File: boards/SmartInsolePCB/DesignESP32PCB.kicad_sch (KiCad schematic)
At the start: 59 parts, among them J1 PJS008U-3000-0, J10 Conn_01x02_Pin, J11 Conn_01x02_Pin, J12 Conn_01x02_Pin, J13 Conn_01x05_Socket, J2 Conn_01x02_Pin, J3 Conn_01x02_Pin, J4 Conn_01x02_Pin, J5 Conn_01x02_Pin, J6 Conn_01x02_Pin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

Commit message: added footprint
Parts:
- added U2: ESP32-S3-WROOM-1, RF_Module:ESP32-S3-WROOM-1, symbol RF_Module:ESP32-S3-WROOM-1
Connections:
- net 3V3: now also U2.2 (3V3)
- net CS: now also U2.21 (IO13)
- net ESP32_EN: now also U2.3 (EN)
- net End Hike: now also U2.35 (IO42)
- net GND: now also U2.1 (GND), U2.40 (GND), U2.41 (GND)
- net GPIO0_STRAPPING: now also U2.27 (IO0)
- net GPIO1: now also U2.10 (IO17)
- net GPIO10: now also U2.23 (IO21)
- net GPIO11: now also U2.20 (IO12)
- net GPIO12: now also U2.7 (IO7)
- net GPIO2: now also U2.11 (IO18)
- net GPIO21: now also U2.12 (IO8)
- net GPIO3: now also U2.19 (IO11)
- net GPIO3_STRAPPING: now also U2.15 (IO3)
- net GPIO46_STRAPPING: now also U2.16 (IO46)
- net GPIO47: now also U2.24 (IO47)
- net GPIO6: now also U2.18 (IO10)
- net GPIO7: now also U2.17 (IO9)
- net GPIO8: now also U2.6 (IO6)
- net MISO: now also U2.9 (IO16)
- net MOSI: now also U2.22 (IO14)
- net RX: now also U2.36 (RXD0)
- net SCLK: now also U2.8 (IO15)
- net SCL_6050: now also U2.13 (IO19), U2.14 (IO20)
- net Start Hike: now also U2.34 (IO41)
- net TX: now also U2.37 (TXD0)
- net USB_N: now also U2.26 (IO45)
- net USB_P: now also U2.25 (IO48)
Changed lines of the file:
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@@
+	)
+	(symbol
+		(lib_id "RF_Module:ESP32-S3-WROOM-1")
+		(at 153.67 60.96 0)
+		(unit 1)
+		(exclude_from_sim no)
+		(in_bom yes)
+		(on_board yes)
+		(dnp no)
+		(fields_autoplaced yes)
+		(property "Reference" "U2"
+			(at 155.8641 30.48 0)
+			(effects
+				(font
+					(size 1.27 1.27)
+				)
+				(justify left)
+			)
+		)
+		(property "Value" "ESP32-S3-WROOM-1"
+			(at 155.8641 33.02 0)
+			(effects
+				(font
+					(size 1.27 1.27)
+				)
+				(justify left)
+			)
+		)
+		(property "Footprint" "RF_Module:ESP32-S3-WROOM-1"
+			(at 153.67 58.42 0)
+			(effects
+				(font
+					(size 1.27 1.27)
+				)
+				(hide yes)
+			)
+		)
+		(property "Datasheet" "https://www.espressif.com/sites/default/files/documentation/esp32-s3-wroom-1_wroom-1u_datasheet_en.pdf"
+			(at 153.67 60.96 0)
+			(effects
+				(font
+					(size 1.27 1.27)
+				)
+				(hide yes)
+			)
+		)
+		(property "Description" "RF Module, ESP32-S3 SoC, Wi-Fi 802.11b/g/n, Bluetooth, BLE, 32-bit, 3.3V, onboard antenna, SMD"
+			(at 153.67 60.96 0)
+			(effects
+				(font
+					(size 1.27 1.27)
+				)
+				(hide yes)
+			)
+		)
+		(pin "26"
+		)
+		(pin "1"
+		)
+		(pin "17"
+		)
+		(pin "18"
+		)
+		(pin "29"
+		)
+		(pin "5"
+		)
+		(pin "37"
+		)
+		(pin "9"
+		)
+		(pin "22"
+		)
+		(pin "36"
+		)
+		(pin "24"
+		)
+		(pin "16"
+		)
+		(pin "12"
+		)
+		(pin "21"
+		)
+		(pin "11"
+		)
+		(pin "39"
+		)
+		(pin "32"
+		)
+		(pin "31"
+		)
+		(pin "41"
+		)
+		(pin "13"
+		)
+		(pin "15"
+		)
+		(pin "28"
+		)
+		(pin "20"
+		)
+		(pin "6"
+		)
+		(pin "2"
+		)
+		(pin "14"
+		)
+		(pin "30"
+		)
+		(pin "40"
+		)
+		(pin "3"
+		)
+		(pin "38"
+		)
+		(pin "7"
+		)
+		(pin "8"
+		)
+		(pin "10"
+		)
+		(pin "34"
+		)
+		(pin "23"
+		)
+		(pin "25"
+		)
+		(pin "33"
+		)
+		(pin "27"
+		)
+		(pin "19"
+		)
+		(pin "4"
+		)
+		(pin "35"
+		)
+		(instances
+			(project "DesignESP32PCB"
+				(path "/6ab99d2f-b2da-4c6e-b437-3c51d85d9865"
+					(reference "U2")
+					(unit 1)
+				)
+			)
+		)
 	)
 	(symbol

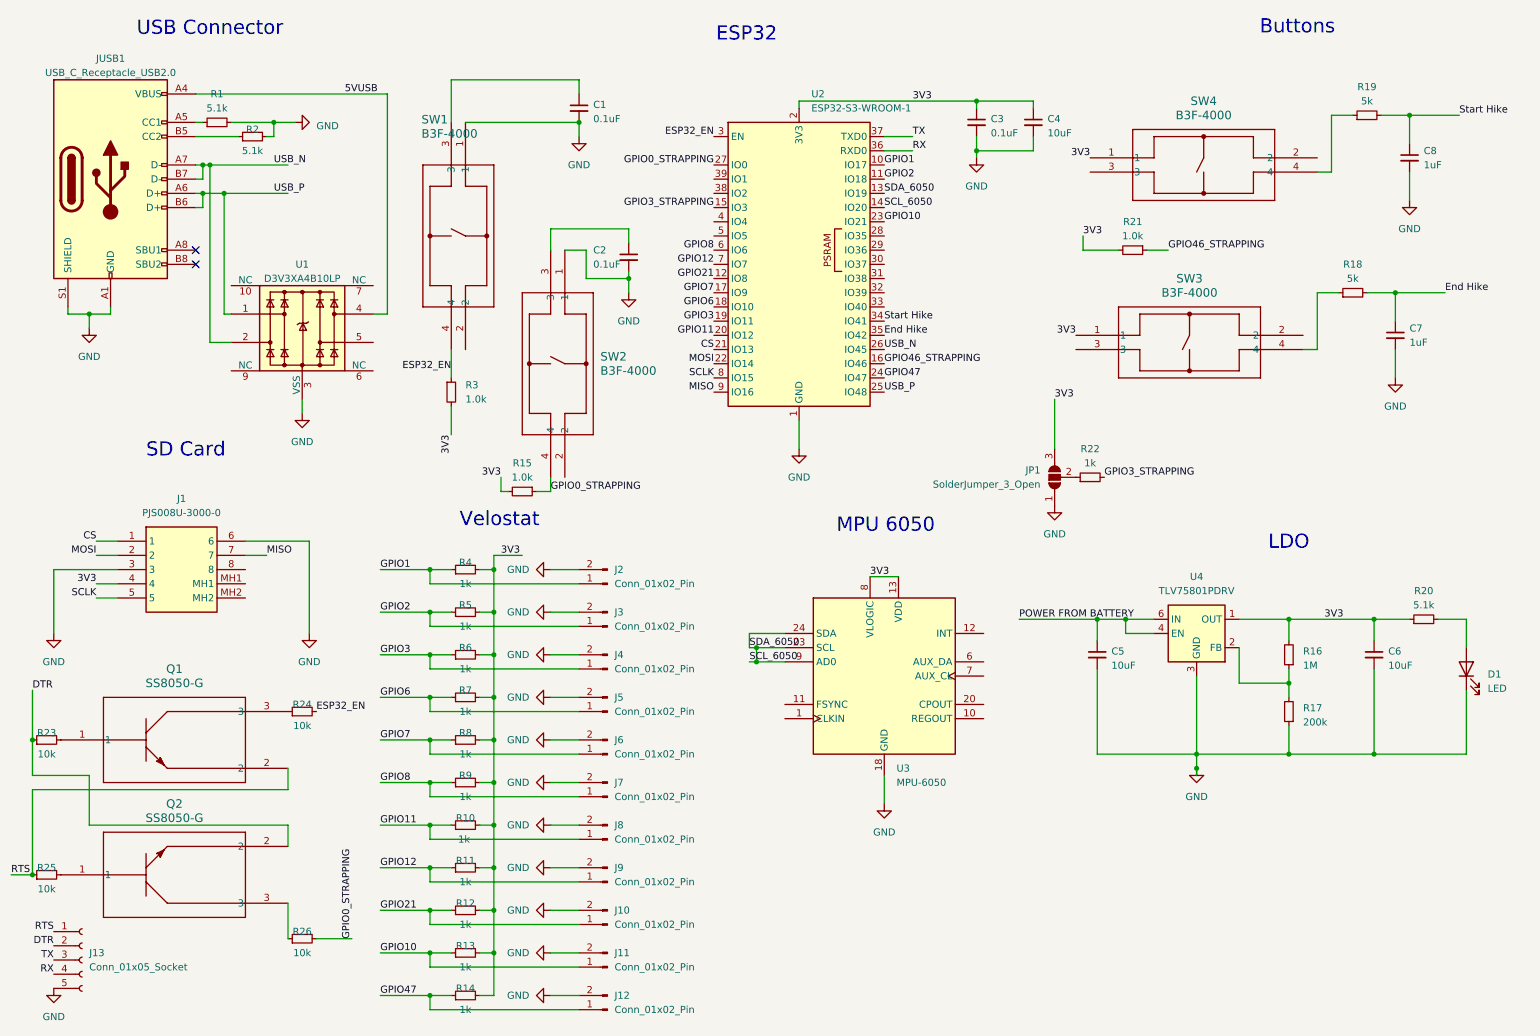
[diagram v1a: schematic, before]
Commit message: routed all connections
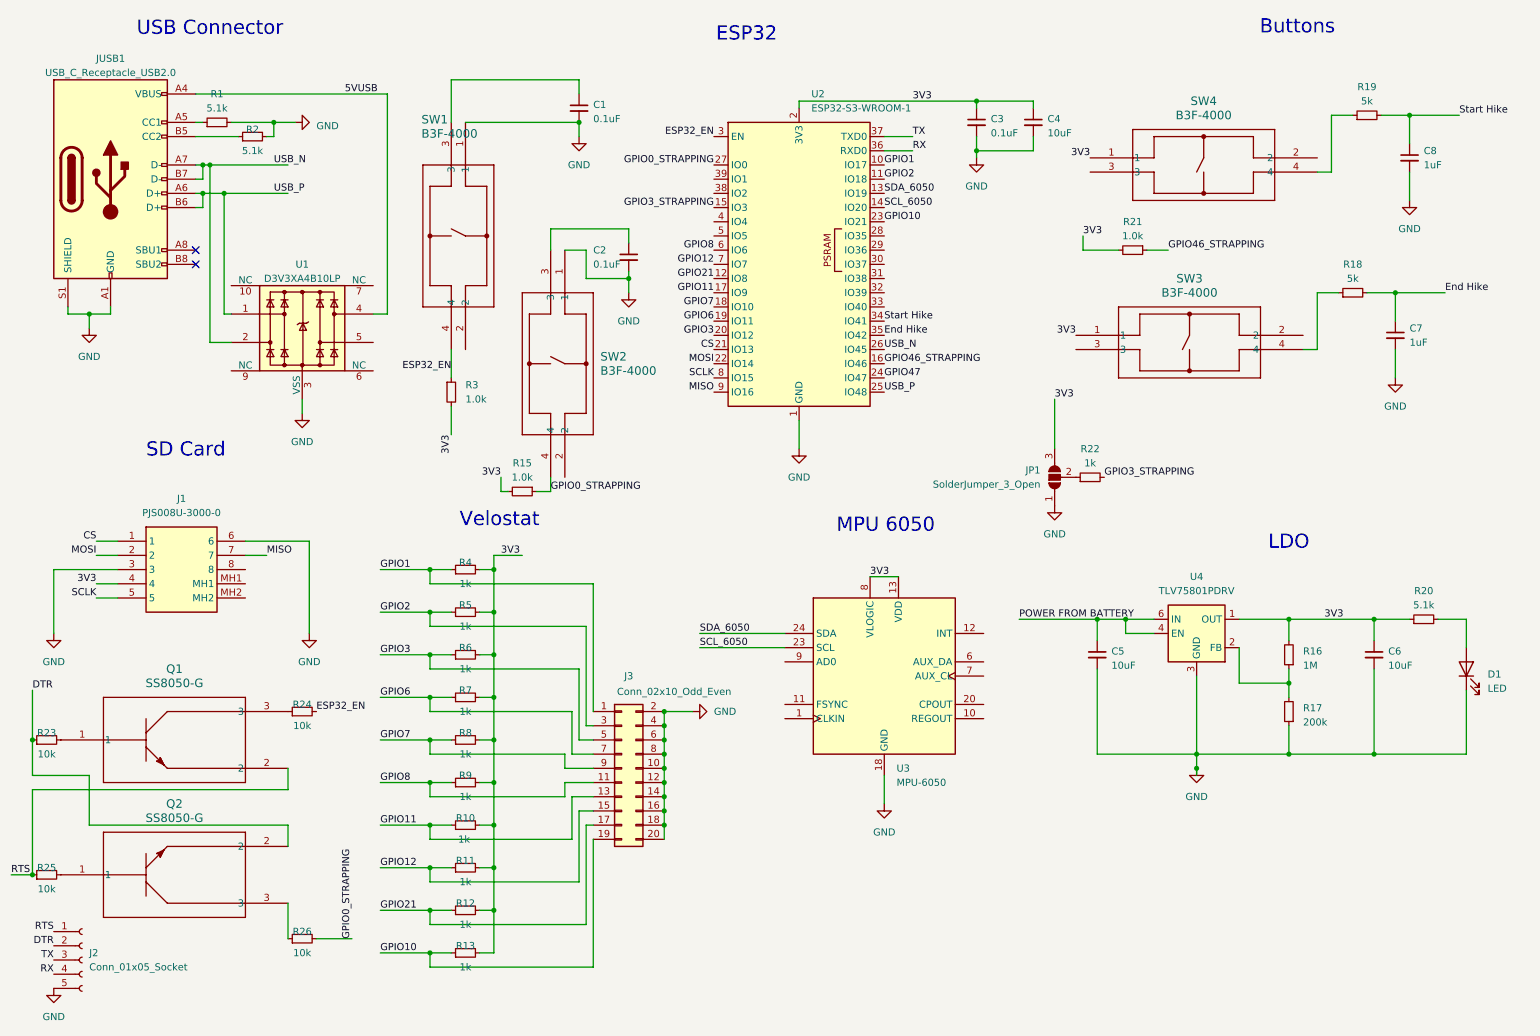
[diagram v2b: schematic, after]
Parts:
- removed J10, J11, J12, J2, J3, J4, J5, J6, J7, J8, J9: Conn_01x02_Pin, Connector_PinHeader_1.00mm:PinHeader_1x02_P1.00mm_Vertical, symbol Connector:Conn_01x02_Pin
- removed R14: 1k, Resistor_SMD:R_0603_1608Metric, symbol Device:R_Small
- added J3: Conn_02x10_Odd_Even, Connector_PinHeader_2.54mm:PinHeader_2x10_P2.54mm_Vertical, symbol Connector_Generic:Conn_02x10_Odd_Even
- J2: renamed from J13; footprint Connector_PinHeader_1.00mm:PinHeader_1x05_P1.00mm_Vertical_SMD_Pin1Left -> Connector_PinHeader_2.54mm:PinHeader_1x05_P2.54mm_Vertical
- JP1: footprint Jumper:SolderJumper-3_P2.0mm_Open_TrianglePad1.0x1.5mm -> Jumper:SolderJumper-3_P1.3mm_Open_RoundedPad1.0x1.5mm
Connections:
- net GND: now also J3.10 (Pin_10), J3.12 (Pin_12), J3.14 (Pin_14), J3.16 (Pin_16), J3.18 (Pin_18), J3.2 (Pin_2), J3.20 (Pin_20), J3.4 (Pin_4), J3.6 (Pin_6), J3.8 (Pin_8)
- net GPIO1: now also J3.1 (Pin_1)
- net GPIO10: now also J3.19 (Pin_19)
- net GPIO11: now also U2.17 (IO9), J3.13 (Pin_13); no longer U2.20 (IO12)
- net GPIO12: now also J3.15 (Pin_15)
- net GPIO2: now also J3.3 (Pin_3)
- net GPIO21: now also J3.17 (Pin_17)
- net GPIO3: now also U2.20 (IO12), J3.5 (Pin_5); no longer U2.19 (IO11)
- net GPIO6: now also U2.19 (IO11), J3.7 (Pin_7); no longer U2.18 (IO10)
- net GPIO7: now also U2.18 (IO10), J3.9 (Pin_9); no longer U2.17 (IO9)
- net GPIO8: now also J3.11 (Pin_11)
- net SCL_6050: no longer U2.13 (IO19), U3.24 (SDA), U3.9 (AD0)
- new net SDA_6050: U2.13 (IO19), U3.24 (SDA)

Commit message: changes
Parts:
- added J4: Conn_01x02_Pin, Connector_JST:JST_PH_B2B-PH-K_1x02_P2.00mm_Vertical, symbol Connector:Conn_01x02_Pin
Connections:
- net GND: now also J4.2 (Pin_2)
- net POWER FROM BATTERY: now also J4.1 (Pin_1)
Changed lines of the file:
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@@
 	)
 	(junction
+		(at 251.46 100.33)
+		(diameter 0)
+		(color 0 0 0 0)
+	)
+	(junction
 		(at 123.19 63.5)
 		(diameter 0)
@@
 	(wire
 		(pts
+			(xy 251.46 100.33) (xy 251.46 101.6)
+		)
+		(stroke
+			(width 0)
+			(type default)
+		)
+	)
+	(wire
+		(pts
 			(xy 115.57 63.5) (xy 123.19 63.5)
 		)
@@
 		)
 	)
+	(label "POWER FROM BATTERY"
+		(at 251.46 97.79 0)
+		(fields_autoplaced yes)
+		(effects
+			(font
+				(size 1.27 1.27)
+			)
+			(justify left bottom)
+		)
+	)
 	(label "CS"
 		(at 27.94 110.49 180)
@@
 	)
 	(symbol
+		(lib_id "power:GND")
+		(at 251.46 100.33 0)
+		(unit 1)
+		(exclude_from_sim no)
+		(in_bom yes)
+		(on_board yes)
+		(dnp no)
+		(fields_autoplaced yes)
+		(property "Reference" "#PWR07"
+			(at 251.46 106.68 0)
+			(effects
+				(font
+					(size 1.27 1.27)
+				)
+				(hide yes)
+			)
+		)
+		(property "Value" "GND"
+			(at 251.46 105.41 0)
+			(effects
+				(font
+					(size 1.27 1.27)
+				)
+			)
+		)
+		(property "Footprint" ""
+			(at 251.46 100.33 0)
+			(effects
+				(font
+					(size 1.27 1.27)
+				)
+				(hide yes)
+			)
+		)
+		(property "Datasheet" ""
+			(at 251.46 100.33 0)
+			(effects
+				(font
+					(size 1.27 1.27)
+				)
+				(hide yes)
+			)
+		)
+		(property "Description" ""
+			(at 251.46 100.33 0)
+			(effects
+				(font
+					(size 1.27 1.27)
+				)
+				(hide yes)
+			)
+		)
+		(pin "1"
+		)
+		(instances
+			(project "DesignESP32PCB"
+				(path "/6ab99d2f-b2da-4c6e-b437-3c51d85d9865"
+					(reference "#PWR07")
+					(unit 1)
+				)
+			)
+		)
+	)
+	(symbol
 		(lib_id "Device:C_Small")
 		(at 256.54 130.81 0)
@@
 					(unit 1)
 				)
+			)
+		)
+	)
+	(symbol
+		(lib_id "Connector:Conn_01x02_Pin")
+		(at 246.38 97.79 0)
+		(unit 1)
+		(exclude_from_sim no)
+		(in_bom yes)
+		(on_board yes)
+		(dnp no)
+		(fields_autoplaced yes)
+		(property "Reference" "J4"
+			(at 247.015 92.71 0)
+			(effects
+				(font
+					(size 1.27 1.27)
+				)
+			)
+		)
+		(property "Value" "Conn_01x02_Pin"
+			(at 247.015 95.25 0)
+			(effects
+				(font
+					(size 1.27 1.27)
+				)
+			)
+		)
+		(property "Footprint" "Connector_JST:JST_PH_B2B-PH-K_1x02_P2.00mm_Vertical"
+			(at 246.38 97.79 0)
+			(effects
+				(font
+					(size 1.27 1.27)
+				)
+				(hide yes)
+			)
+		)
+		(property "Datasheet" "~"
+			(at 246.38 97.79 0)
+			(effects
+				(font
+					(size 1.27 1.27)
+				)
+				(hide yes)
+			)
+		)
+		(property "Description" "Generic connector, single row, 01x02, script generated"
+			(at 246.38 97.79 0)
+			(effects
+				(font
+					(size 1.27 1.27)
+				)
+				(hide yes)
+			)
+		)
+		(pin "1"
+		)
+		(pin "2"
+		)
+		(instances
+			(project "DesignESP32PCB"
+				(path "/6ab99d2f-b2da-4c6e-b437-3c51d85d9865"
+					(reference "J4")
+					(unit 1)
+				)
